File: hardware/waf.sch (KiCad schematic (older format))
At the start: 0 parts

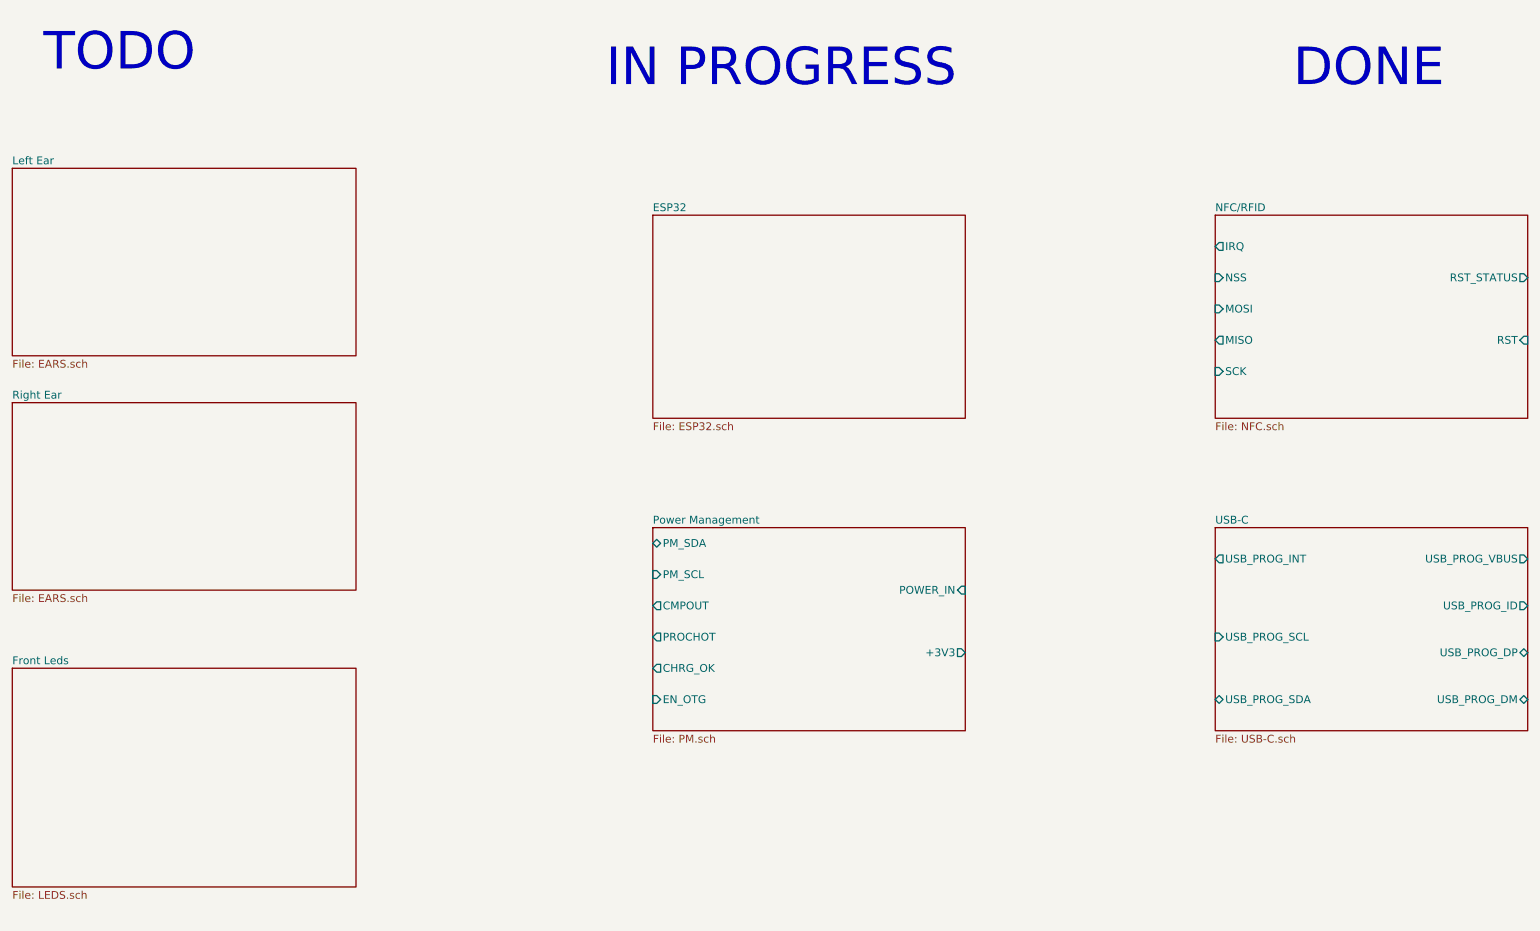
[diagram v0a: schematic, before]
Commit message: Add LED column and instanciate 32 of them
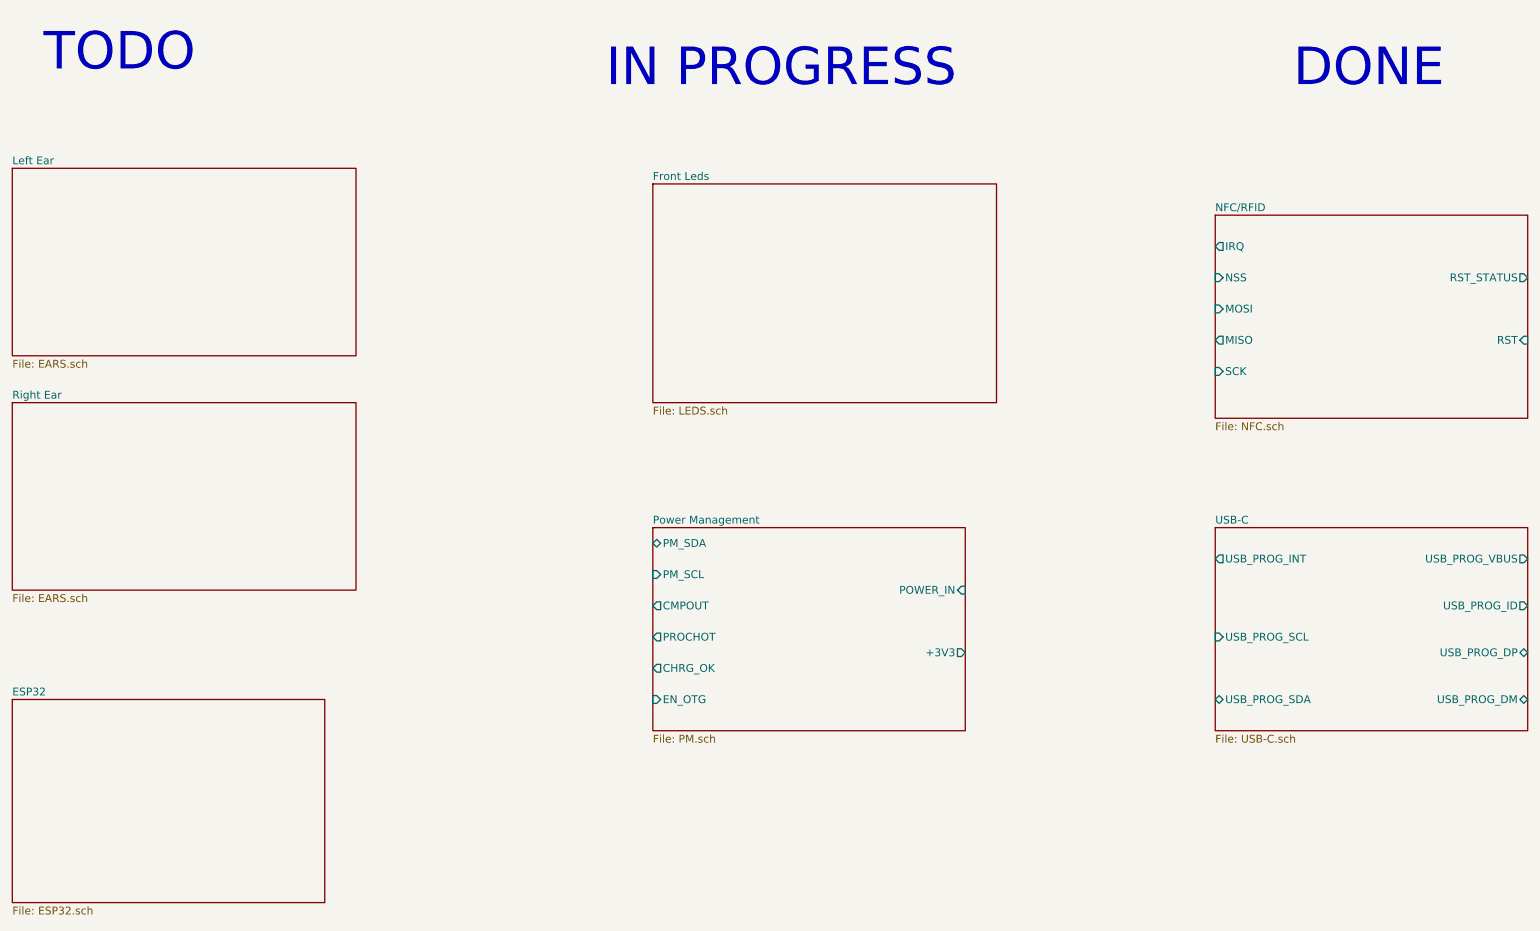
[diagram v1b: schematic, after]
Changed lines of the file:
@@
 $Descr A4 11693 8268
 encoding utf-8
-Sheet 1 8
+Sheet 1 40
 Title "WAF WAF Howling badge"
 Date ""
@@
 IN PROGRESS
 $Sheet
-S 4800 2000 2000 1300
+S 700  5100 2000 1300
 U 5C65C087
 F0 "ESP32" 50
@@
 $EndSheet
 $Sheet
-S 700  4900 2200 1400
+S 4800 1800 2200 1400
 U 5CC10402
 F0 "Front Leds" 50

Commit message: Add LEDs column drivers
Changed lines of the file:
@@
 $Descr A4 11693 8268
 encoding utf-8
-Sheet 1 40
+Sheet 1 44
 Title "WAF WAF Howling badge"
 Date ""
@@
 $EndDescr
 $Sheet
-S 8400 4000 2000 1300
+S 8400 3600 2000 1300
 U 5C6D04B5
 F0 "USB-C" 50
 F1 "USB-C.sch" 50
-F2 "USB_PROG_DM" B R 10400 5100 50
-F3 "USB_PROG_DP" B R 10400 4800 50
-F4 "USB_PROG_ID" O R 10400 4500 50
-F5 "USB_PROG_INT" O L 8400 4200 50
-F6 "USB_PROG_SCL" I L 8400 4700 50
-F7 "USB_PROG_SDA" B L 8400 5100 50
-F8 "USB_PROG_VBUS" O R 10400 4200 50
+F2 "USB_PROG_DM" B R 10400 4700 50
+F3 "USB_PROG_DP" B R 10400 4400 50
+F4 "USB_PROG_ID" O R 10400 4100 50
+F5 "USB_PROG_INT" O L 8400 3800 50
+F6 "USB_PROG_SCL" I L 8400 4300 50
+F7 "USB_PROG_SDA" B L 8400 4700 50
+F8 "USB_PROG_VBUS" O R 10400 3800 50
 $EndSheet
 $Sheet
@@
 $EndSheet
 $Sheet
-S 4800 4000 2000 1300
+S 4800 2000 2000 1200
 U 5C7B1A3B
 F0 "Power Management" 50
 F1 "PM.sch" 50
-F2 "POWER_IN" I R 6800 4400 50
-F3 "+3V3" O R 6800 4800 50
-F4 "PM_SDA" B L 4800 4100 50
-F5 "PM_SCL" I L 4800 4300 50
-F6 "PROCHOT" O L 4800 4700 50
-F7 "CHRG_OK" O L 4800 4900 50
-F8 "EN_OTG" I L 4800 5100 50
-F9 "CMPOUT" O L 4800 4500 50
+F2 "POWER_IN" I R 6800 2400 50
+F3 "+3V3" O R 6800 2800 50
+F4 "PM_SDA" B L 4800 2100 50
+F5 "PM_SCL" I L 4800 2300 50
+F6 "PROCHOT" O L 4800 2700 50
+F7 "CHRG_OK" O L 4800 2900 50
+F8 "EN_OTG" I L 4800 3100 50
+F9 "CMPOUT" O L 4800 2500 50
 $EndSheet
 $Sheet
-S 4800 1800 2200 1400
+S 8400 5200 2000 1000
 U 5CC10402
 F0 "Front Leds" 50
 F1 "LEDS.sch" 50
+F2 "ROW_GCLK" I L 8400 5300 50
+F3 "ROW_LAT" I L 8400 5900 50
+F4 "ROW_SCLK" I L 8400 5500 50
+F5 "ROW_SIN" I L 8400 5700 50
+F6 "ROW_SOUT" O L 8400 6100 50
+F7 "COL_nSRCLR" I R 10400 6100 50
+F8 "COL_nOE" I R 10400 5900 50
+F9 "COL_SRCLK" I R 10400 5500 50
+F10 "COL_RCLK" I R 10400 5300 50
+F11 "COL_SER" I R 10400 5700 50
 $EndSheet
 $EndSCHEMATC

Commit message: Place BQ25892
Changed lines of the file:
@@
 F0 "Power Management" 50
 F1 "PM.sch" 50
-F2 "POWER_IN" I R 6800 2400 50
-F3 "+3V3" O R 6800 2800 50
-F4 "PM_SDA" B L 4800 2100 50
-F5 "PM_SCL" I L 4800 2300 50
-F6 "PROCHOT" O L 4800 2700 50
-F7 "CHRG_OK" O L 4800 2900 50
-F8 "EN_OTG" I L 4800 3100 50
-F9 "CMPOUT" O L 4800 2500 50
+F2 "POWER_IN" I R 6800 2600 50
+F3 "PM_SDA" B L 4800 2100 50
+F4 "PM_SCL" I L 4800 2300 50
+F5 "PROCHOT" O L 4800 2700 50
+F6 "CHRG_OK" O L 4800 2900 50
+F7 "EN_OTG" I L 4800 3100 50
+F8 "CMPOUT" O L 4800 2500 50
 $EndSheet
 $Sheet
